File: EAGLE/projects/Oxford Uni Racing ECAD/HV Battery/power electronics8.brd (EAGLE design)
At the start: 165.9 x 104.3 mm, 62 parts, among them IC1 4043D, IC2 SE555D, IC6 4011D, K1 T9AS1D12-48=T9A, K2 T9AS5D12-12=T9A, K3 T9AS1D12-48=T9A, K4 T9AS1D12-48=T9A, K5 T9AS1D12-48=T9A, Q1 BSS138, Q2 BSS138, Q3 BSS138

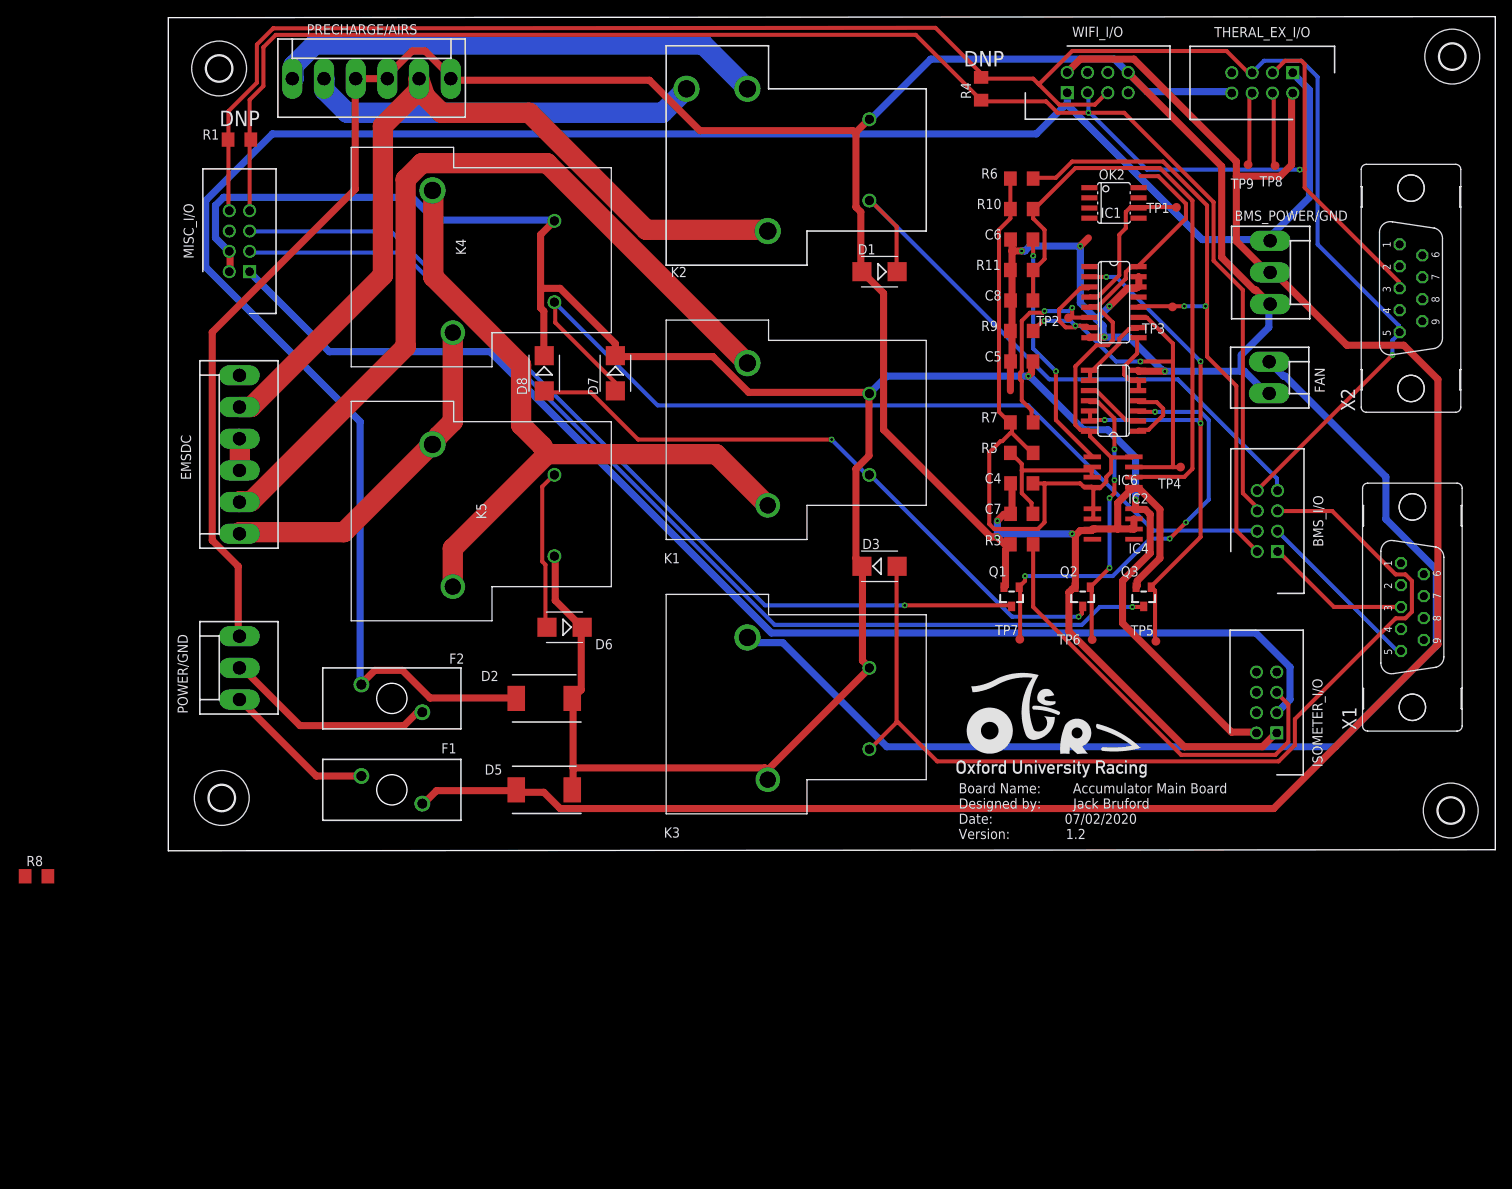
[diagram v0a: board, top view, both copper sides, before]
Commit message: created power_electronics8 which is a design for a revised board including mosfets to isolate the 3.3v and 12v rails via charge safe and discharge enable signal nets. Also fixed naming issues with those signals
Signed-off-by: Jack Bruford <jack.bruford41@gmail.com>
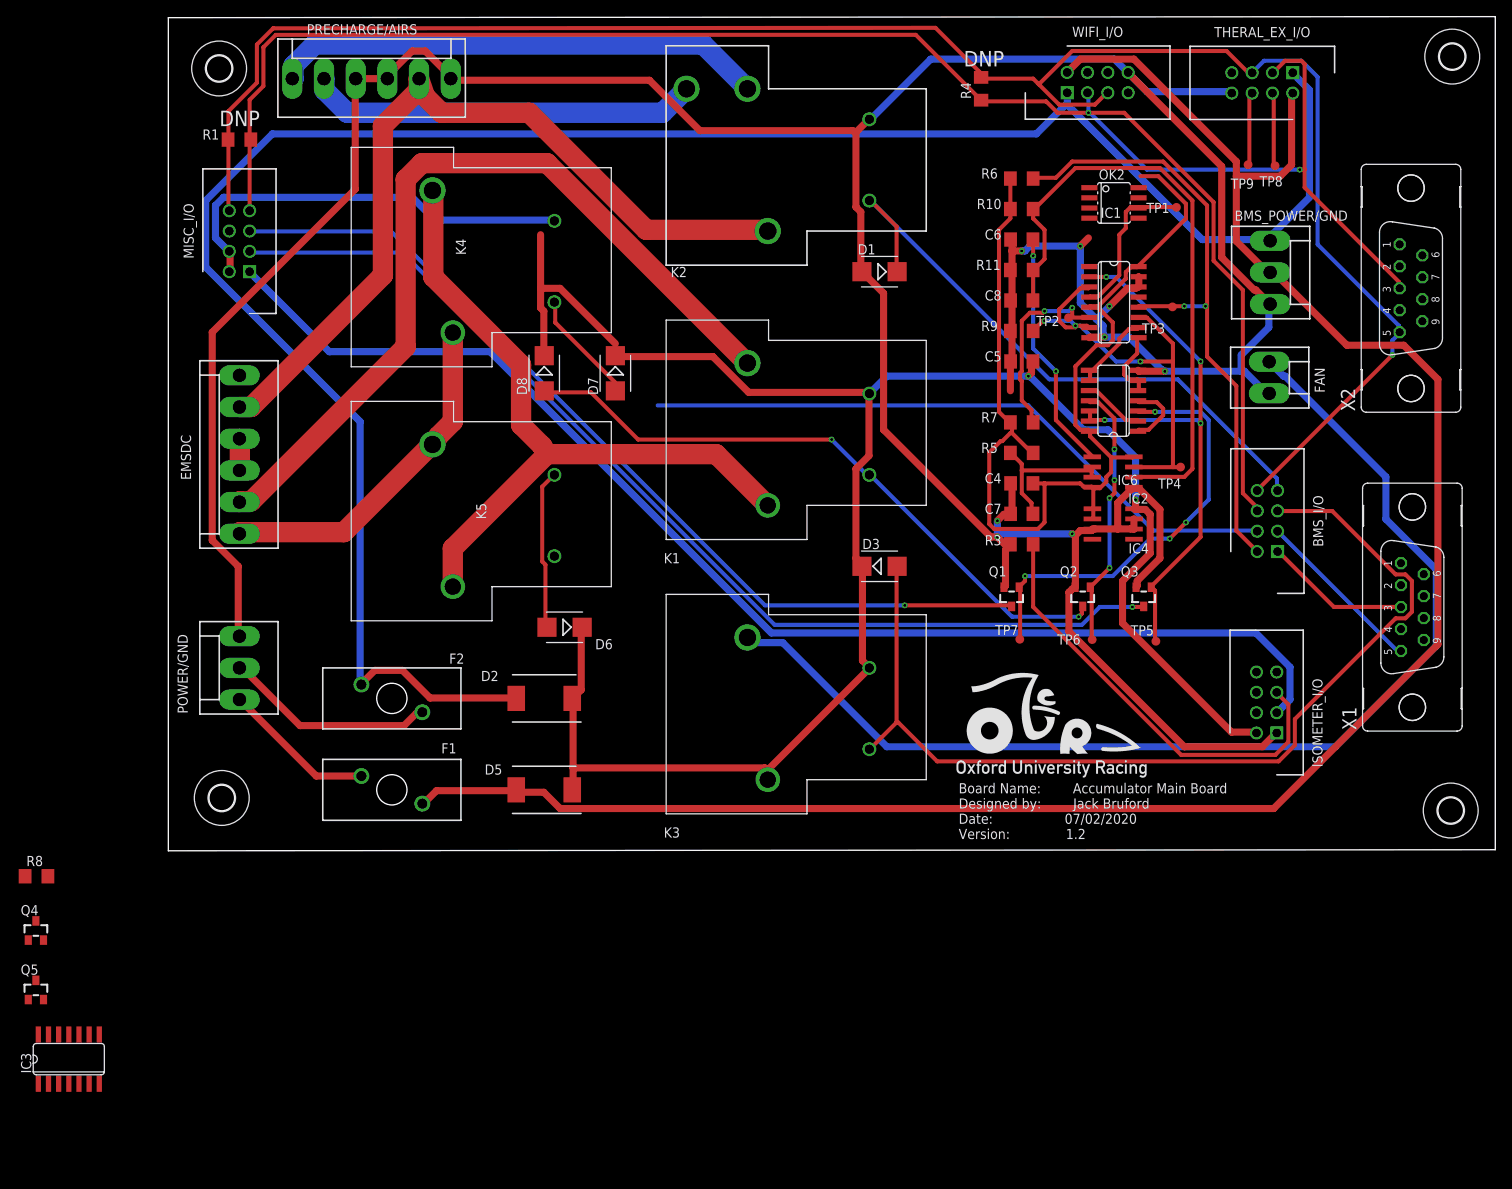
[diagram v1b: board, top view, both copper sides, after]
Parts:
- added IC3: 4011D, 40xx:SO14
- added Q4, Q5: BSS138, m-pad-2.1:SOT23
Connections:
- removed net CHG_SAFE: BMS_I/O.2, IC1.12, R6.2, TP3.TP
- new net N$16: IC3.4, Q4.1
- new net N$18: IC3.3, Q5.1
- new net N$6: D7.A, K4.2, Q4.3
- new net N$9: D6.A, K5.1, Q5.3
- net +3V3: now also IC3.14
- net CHARGE_SAFE: now also BMS_I/O.2, IC1.12, IC3.1, IC3.2, R6.2, TP3.TP; no longer D6.A, K5.1
- net DISCHARGE_ENABLE: now also IC3.5, IC3.6; no longer D7.A, K4.2
- net GND: now also IC3.7, Q4.2, Q5.2
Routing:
- net CHG_SAFE: track 79.5 -> 0.00 mm, vias 2 -> 0
- net CHARGE_SAFE: track 20.0 -> 79.3 mm, vias 0 -> 2
- net DISCHARGE_ENABLE: track 138.5 -> 106.0 mm
- net N$9: track 0.00 -> 20.0 mm
- net +12V: track 316.7 -> 301.6 mm
- net N$6: track 0.00 -> 14.2 mm

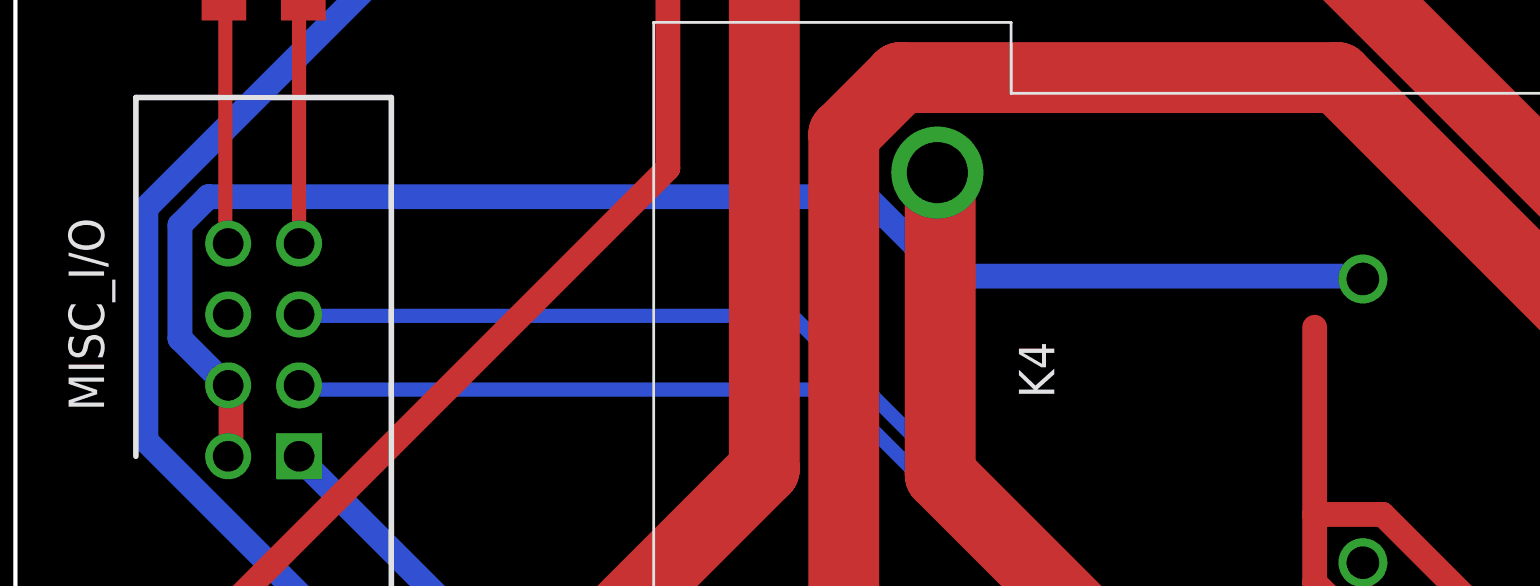
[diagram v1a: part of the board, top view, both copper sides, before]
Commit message: connected CAN 1 to misc pcb connector allowing it to be fed to the lv pack connector. This was missing. This has also meant having a single 12V output for both the IMD and AMS warning lights
Signed-off-by: Jack Bruford <jack.bruford41@gmail.com>
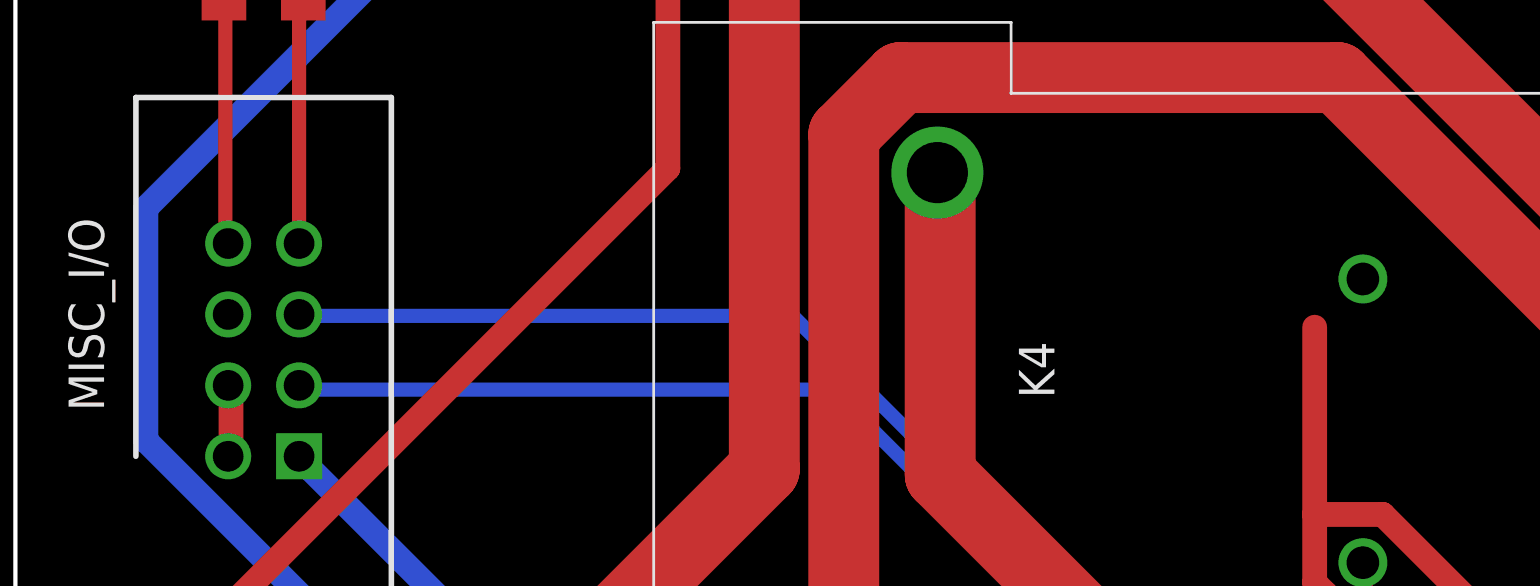
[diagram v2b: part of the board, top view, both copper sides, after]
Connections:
- net +12V: no longer MISC_I/O.4
- net CAN1_H: now also MISC_I/O.4
- net CAN1_L: now also MISC_I/O.6
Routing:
- net +12V: track 301.6 -> 251.1 mm
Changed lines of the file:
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@@
 <contactref element="K1" pad="1"/>
 <contactref element="MISC_I/O" pad="2"/>
-<contactref element="MISC_I/O" pad="4"/>
 <contactref element="K3" pad="1"/>
 <contactref element="K3" pad="3"/>
@@
 <wire x1="7.7216" y1="74.7776" x2="7.7216" y2="72.5424" width="0.889" layer="1"/>
 <wire x1="7.7216" y1="72.5424" x2="7.62" y2="72.39" width="0.889" layer="1"/>
-<wire x1="7.7216" y1="74.7776" x2="7.62" y2="74.93" width="0.889" layer="1"/>
 <wire x1="46.9392" y1="67.4624" x2="46.9392" y2="61.976" width="0.889" layer="1"/>
 <wire x1="46.5328" y1="67.8688" x2="46.9392" y2="67.4624" width="0.889" layer="1"/>
@@
 <wire x1="48.9712" y1="70.3072" x2="55.88" y2="63.3984" width="0.889" layer="1"/>
 <wire x1="46.5328" y1="70.3072" x2="48.9712" y2="70.3072" width="0.889" layer="1"/>
-<wire x1="5.8928" y1="76.6064" x2="7.5184" y2="74.9808" width="0.889" layer="16"/>
-<wire x1="5.8928" y1="80.6704" x2="5.8928" y2="76.6064" width="0.889" layer="16"/>
-<wire x1="6.9088" y1="81.6864" x2="5.8928" y2="80.6704" width="0.889" layer="16"/>
-<wire x1="30.48" y1="81.6864" x2="6.9088" y2="81.6864" width="0.889" layer="16"/>
-<wire x1="33.3248" y1="78.8416" x2="30.48" y2="81.6864" width="0.889" layer="16"/>
-<wire x1="48.1584" y1="78.8416" x2="33.3248" y2="78.8416" width="0.889" layer="16"/>
-<wire x1="7.5184" y1="74.9808" x2="7.62" y2="74.93" width="0.889" layer="16"/>
 <wire x1="122.1232" y1="42.672" x2="120.904" y2="42.672" width="0.889" layer="1"/>
 <wire x1="122.7328" y1="42.0624" x2="122.1232" y2="42.672" width="0.889" layer="1"/>
@@
 <contactref element="K5" pad="2"/>
 <contactref element="D6" pad="C"/>
-<wire x1="48.1584" y1="78.8416" x2="48.26" y2="78.74" width="0" layer="19" extent="16-16"/>
 <wire x1="46.5328" y1="77.0128" x2="48.26" y2="78.74" width="0" layer="19" extent="1-1"/>
 <wire x1="55.88" y1="61.89" x2="55.88" y2="63.3984" width="0" layer="19" extent="1-1"/>
@@
 <wire x1="51.73" y1="27.94" x2="51.6128" y2="27.8384" width="0" layer="19" extent="1-1"/>
 <wire x1="48.26" y1="36.83" x2="51.73" y2="27.94" width="0" layer="19" extent="1-1"/>
+<wire x1="7.7216" y1="74.7776" x2="46.5328" y2="77.0128" width="0" layer="19" extent="1-1"/>
 </signal>
 <signal name="M_HS">
@@
 <wire x1="154.0256" y1="30.48" x2="154.08275" y2="30.46095" width="0.508" layer="1"/>
 <wire x1="138.7856" y1="37.3888" x2="138.65225" y2="37.40785" width="0.508" layer="1"/>
+<contactref element="MISC_I/O" pad="4"/>
+<wire x1="7.62" y1="74.93" x2="138.65225" y2="37.40785" width="0" layer="19" extent="1-1"/>
 </signal>
 <signal name="CAN1_L">
@@
 <wire x1="154.0256" y1="24.9936" x2="154.08275" y2="24.97455" width="0.508" layer="16"/>
 <wire x1="138.7856" y1="39.8272" x2="138.65225" y2="39.94785" width="0.508" layer="16"/>
+<contactref element="MISC_I/O" pad="6"/>
+<wire x1="7.62" y1="77.47" x2="138.65225" y2="39.94785" width="0" layer="19" extent="1-1"/>
 </signal>
 <signal name="N$7">

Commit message: changes before laptop dies
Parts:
- added TP10, TP11, TP12: TPSTP11R, testpad:TP11R
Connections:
- net OK_HS: now also TP10.TP
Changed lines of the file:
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@@
 <attribute name="VALUE" x="-15.99565" y="-26.67635" size="1.27" layer="27" ratio="10"/>
+</element>
+<element name="TP10" library="testpad" library_urn="urn:adsk.eagle:library:385" package="TP11R" package3d_urn="urn:adsk.eagle:package:27961/1" value="TPSTP11R" x="-17.907" y="-32.8803" smashed="yes">
+<attribute name="NAME" x="-18.4569" y="-32.2804" size="1.27" layer="25"/>
+<attribute name="TP_SIGNAL_NAME" value="" x="-17.907" y="-32.8803" size="1.778" layer="27" display="off"/>
+<attribute name="VALUE" x="-18.415" y="-33.3883" size="0.0254" layer="27"/>
+</element>
+<element name="TP11" library="testpad" library_urn="urn:adsk.eagle:library:385" package="TP11R" package3d_urn="urn:adsk.eagle:package:27961/1" value="TPSTP11R" x="-17.907" y="-36.32835" smashed="yes">
+<attribute name="NAME" x="-18.4569" y="-35.72845" size="1.27" layer="25"/>
+<attribute name="TP_SIGNAL_NAME" value="" x="-17.907" y="-36.32835" size="1.778" layer="27" display="off"/>
+<attribute name="VALUE" x="-18.415" y="-36.83635" size="0.0254" layer="27"/>
+</element>
+<element name="TP12" library="testpad" library_urn="urn:adsk.eagle:library:385" package="TP11R" package3d_urn="urn:adsk.eagle:package:27961/1" value="TPSTP11R" x="-17.907" y="-39.7764" smashed="yes">
+<attribute name="NAME" x="-18.4569" y="-39.1765" size="1.27" layer="25"/>
+<attribute name="TP_SIGNAL_NAME" value="" x="-17.907" y="-39.7764" size="1.778" layer="27" display="off"/>
+<attribute name="VALUE" x="-18.415" y="-40.2844" size="0.0254" layer="27"/>
 </element>
 </elements>
@@
 <contactref element="ISOMETER_I/O" pad="8"/>
 <contactref element="OK2" pad="2"/>
-<wire x1="115.13185" y1="81.61655" x2="136.017" y2="22.34565" width="0" layer="19" extent="1-1"/>
+<contactref element="TP10" pad="TP"/>
+<wire x1="136.017" y1="22.34565" x2="115.13185" y2="81.61655" width="0" layer="19" extent="1-1"/>
+<wire x1="-17.907" y1="-32.8803" x2="136.017" y2="22.34565" width="0" layer="19" extent="1-1"/>
 </signal>
 <signal name="N$37">
